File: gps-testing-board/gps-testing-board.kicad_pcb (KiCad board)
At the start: 2 copper layers, 29 parts, among them J1 Conn_01x02_Male, J10 U.FL-R-SMT-1_10_, J11 U.FL-R-SMT-1_10_, J12 Conn_01x02_Male, J13 Conn_01x03_Male, J14 Conn_01x02_Male, J15 Conn_01x02_Male, J16 BAT-HLD-001-THM, J17 1066, J2 Conn_01x03_Male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

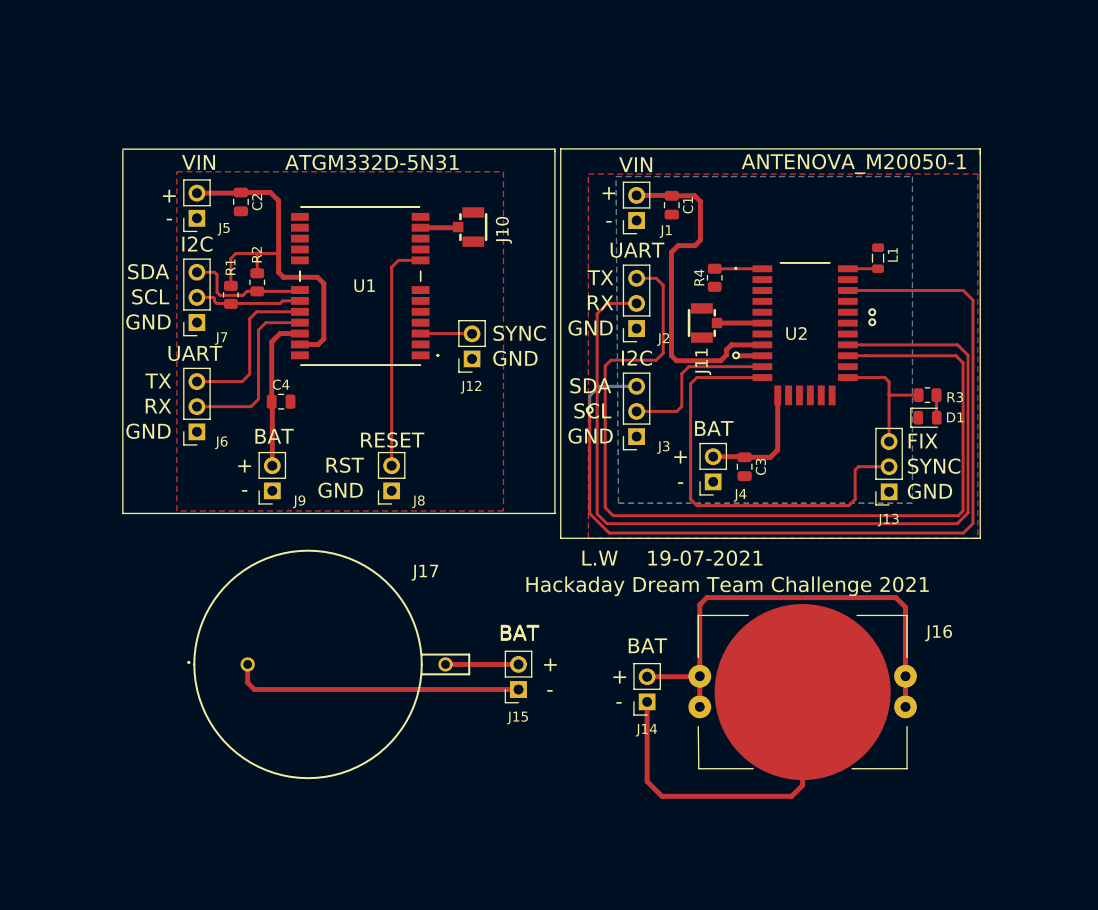
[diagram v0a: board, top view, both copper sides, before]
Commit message: Added 3D models
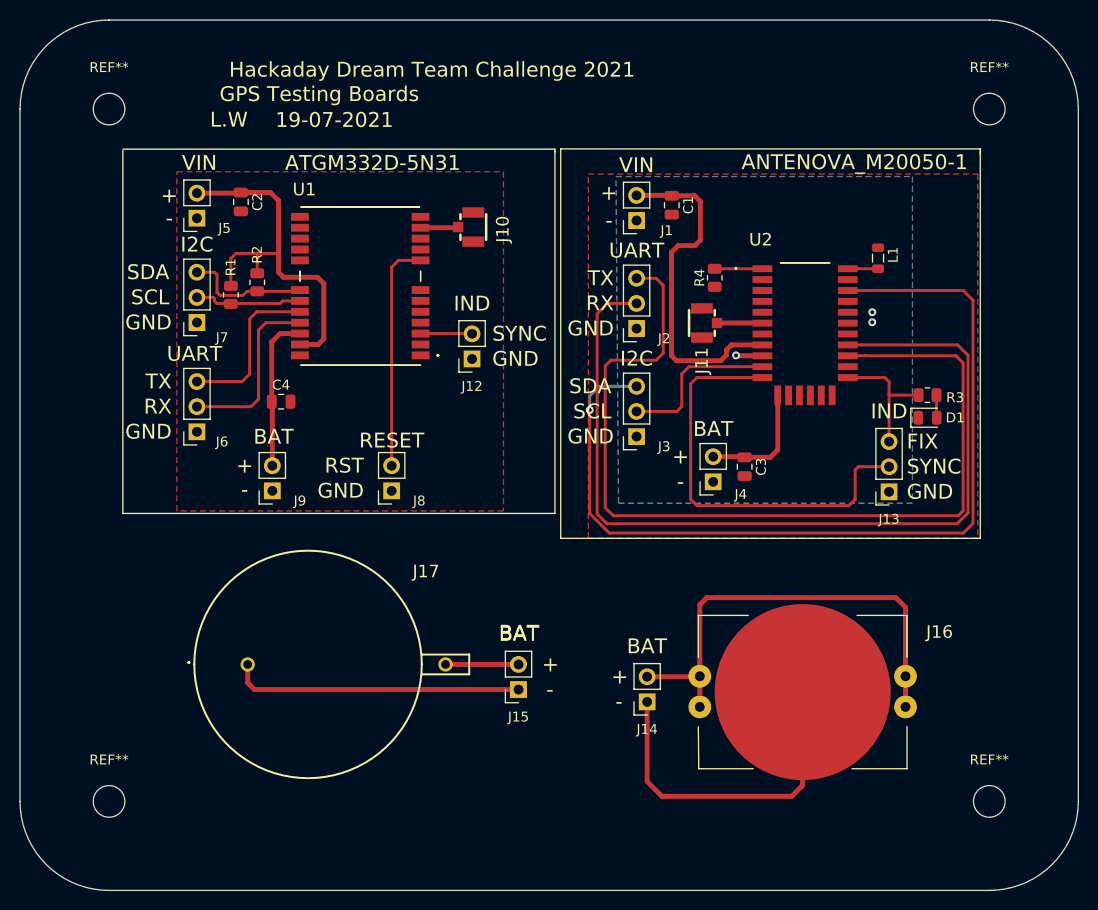
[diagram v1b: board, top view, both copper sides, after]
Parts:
- added REF**: MountingHole_3.2mm_M3, MountingHole:MountingHole_3.2mm_M3, F.Cu at (200.0, 71.0)
- added REF**: MountingHole_3.2mm_M3, MountingHole:MountingHole_3.2mm_M3, F.Cu at (111.0, 71.0)
- added REF**: MountingHole_3.2mm_M3, MountingHole:MountingHole_3.2mm_M3, F.Cu at (200.0, 141.0)
- added REF**: MountingHole_3.2mm_M3, MountingHole:MountingHole_3.2mm_M3, F.Cu at (111.0, 141.0)
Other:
- board outline added: 107 x 88 mm
- board text added: "GPS Testing Boards"
